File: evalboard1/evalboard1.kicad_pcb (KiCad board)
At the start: 2 copper layers, 67.5 x 45.3 mm, 37 parts, among them J1 USB_OTG, J10 Conn_01x12_Male, J11 Conn_01x18_Male, J12 Conn_01x15_Male, J13 Conn_01x03_Male, J14 power select, J2 RX, J3 TX, J4 analog, J5 IO, J6 core, J7 Conn_01x09_Male, J8 Conn_01x06_Male, J9 Conn_01x17_Male, SW1 SW_Push, U1 GA144A12, U2 FT234XD-R, U3 LTC3406ES5-1.8, U4 SST25WF080B, Y1 Crystal

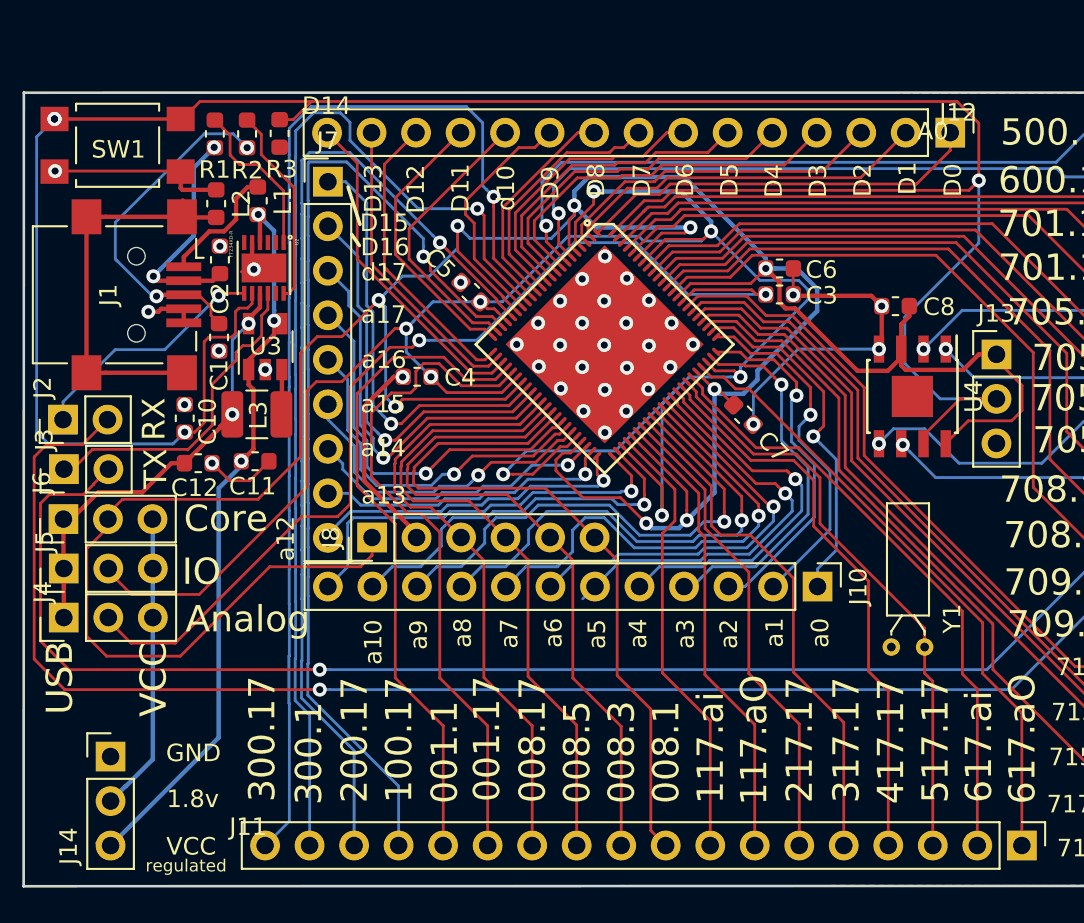
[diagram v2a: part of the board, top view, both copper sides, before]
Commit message: evalboard1: add 5v pin to add-on board header
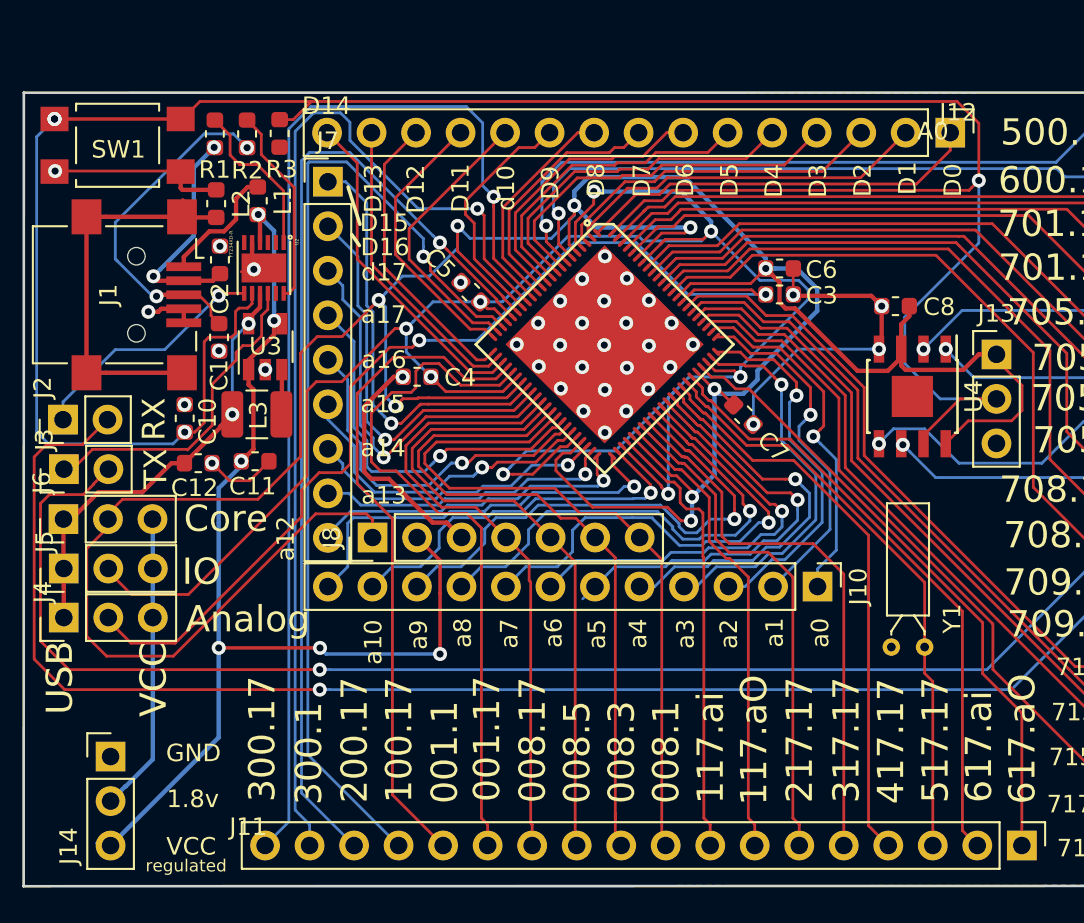
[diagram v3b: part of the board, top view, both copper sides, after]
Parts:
- J8: value Conn_01x06_Male -> Conn_01x07_Male; footprint Connector_PinHeader_2.54mm:PinHeader_1x06_P2.54mm_Vertical -> Connector_PinHeader_2.54mm:PinHeader_1x07_P2.54mm_Vertical
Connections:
- J8 pad 2: GND -> vcc
- J8 pad 3: 008.17 -> GND
- J8 pad 4: 008.5 -> 008.17
- J8 pad 5: 008.3 -> 008.5
- J8 pad 6: 008.1 -> 008.3
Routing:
- net vcc: track 44.3 -> 64.3 mm, vias 3 -> 6
- net vccI: track 124.4 -> 121.5 mm
- net GND: track 52.6 -> 54.7 mm
- net 317.17: track 29.8 -> 31.8 mm
- net 217.17: track 27.6 -> 29.1 mm
- net a6: track 23.7 -> 24.7 mm
- net 001.17: track 38.5 -> 39.5 mm
- net a5: track 24.1 -> 25.0 mm
- net a2: track 20.2 -> 21.1 mm
- net a4: track 22.0 -> 22.8 mm
- net a9: track 28.7 -> 29.5 mm
- net a3: track 21.5 -> 22.3 mm
- net 008.3: track 39.4 -> 40.1 mm
- net a7: track 27.1 -> 27.7 mm

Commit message: update
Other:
- board text added: "GA144 evalboard version 1 github.com/mschuldt/ga144-breakout"
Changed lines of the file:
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@@
-(kicad_pcb (version 20171130) (host pcbnew 5.0.1-33cea8e~68~ubuntu14.04.1)
+(kicad_pcb (version 20171130) (host pcbnew 5.0.2-bee76a0~70~ubuntu14.04.1)
   (general
     (thickness 1.6)
-    (drawings 90)
+    (drawings 91)
     (tracks 1385)
     (zones 0)
@@
     )
   )
+  (gr_text "GA144 evalboard version 1\ngithub.com/mschuldt/ga144-breakout" (at 150.622 110.236) (layer B.SilkS)
+    (effects (font (size 1.5 1.5) (thickness 0.3)) (justify left mirror))
+  )
   (gr_line (start 111.18 80.43) (end 111.18 80.4) (layer B.SilkS) (width 0.2))
